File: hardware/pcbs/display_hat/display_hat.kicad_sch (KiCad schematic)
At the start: 6 parts, among them J1 Conn_02x20_Odd_Even

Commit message: hat_pcbs are almost done
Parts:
- removed J1: Conn_02x20_Odd_Even, Connector_PinHeader_2.54mm:PinHeader_2x20_P2.54mm_Vertical, symbol Connector_Generic:Conn_02x20_Odd_Even
- removed J?: I/O, Library:mta100_01x6_P2.54_647050-6, symbol Connector_Generic:Conn_01x06
- added C1: 1μF, Capacitor_SMD:C_0805_2012Metric, symbol Device:C
- added J1: WAVESHARE_HAT_HEADER, Connector_PinHeader_2.54mm:PinHeader_2x20_P2.54mm_Vertical, symbol conn:waveshare_hat_header
- added J2, J3: Header_01x08, Connector_MTA-100:mta100_01x8_P2.54_640455-8, symbol conn:Conn_01x08
- added J4: MTA100_02, Connector_MTA-100:mta100_01x2_P2.54_640455-2, symbol conn:Screw_Terminal_01x02
- added JP1: PWR FROM SIDE, Connector_PinHeader_2.54mm:PinHeader_1x02_P2.54mm_Vertical, symbol Jumper:Jumper_2_Open
- added JP2: PWR FROM MAIN, Connector_PinHeader_2.54mm:PinHeader_1x02_P2.54mm_Vertical, symbol Jumper:Jumper_2_Open
- added R1: 10kΩ, Resistor_SMD:R_0805_2012Metric, symbol Device:R
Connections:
- net +5V: now also J1.2 (+5V), J1.4 (+5V)
- net GND: now also C1.2, J1.14 (GND), J1.20 (GND), J1.25 (GND), J1.30 (GND), J1.34 (GND), J1.39 (GND), J1.6 (GND), J1.9 (GND), J2.1 (Pin_1), J3.8 (Pin_8), J4.1 (Pin_1)
- new net: J2.8 (Pin_8), JP1.1 (A)
- new net: J3.7 (Pin_7), JP2.1 (A)
- new net +3.3V: C1.1, J1.1 (+3.3V), J1.17 (+3.3V), J4.2 (Pin_2), JP1.2 (B), JP2.2 (B), R1.2
- new net BL: J1.32 (D2_BL), J1.33 (D1_BL), J1.35 (D0_BL), J3.2 (Pin_2), R1.1
- new net MAIN_CLK: J1.40 (D0_CLK), J3.4 (Pin_4)
- new net MAIN_CS: J1.12 (D0_CS), J3.6 (Pin_6)
- new net MAIN_DAT: J1.38 (D0_DAT), J3.3 (Pin_3)
- new net MAIN_DC: J1.15 (D0_DC), J3.5 (Pin_5)
- new net MAIN_RST: J1.13 (D0_RST), J3.1 (Pin_1)
- new net SIDE_CLK: J1.23 (D12_CLK), J2.6 (Pin_6)
- new net SIDE_CS_L: J1.24 (D1_CS), J2.4 (Pin_4)
- new net SIDE_CS_R: J1.26 (D2_CS), J2.5 (Pin_5)
- new net SIDE_DAT: J1.19 (D12_DAT), J2.7 (Pin_7)
- new net SIDE_DC: J1.29 (D2_DC), J1.7 (D1_DC), J2.3 (Pin_3)
- new net SIDE_RST: J1.16 (D2_RST), J1.18 (D1_RST), J2.2 (Pin_2)
- no-connect marks 0 -> 12
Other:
- moved on the sheet: H1, H2, H3, H4

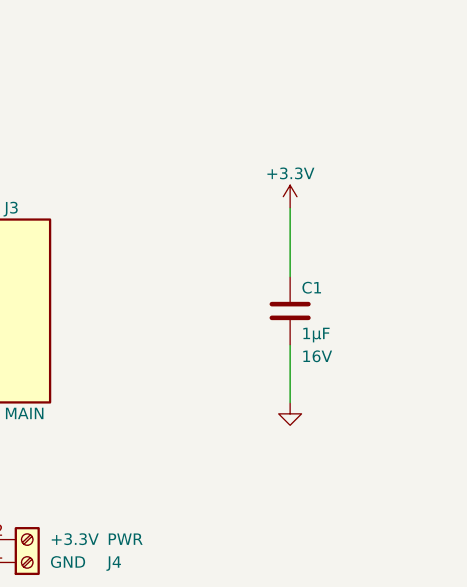
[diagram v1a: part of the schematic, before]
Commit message: hat_pcbs: add some resistors
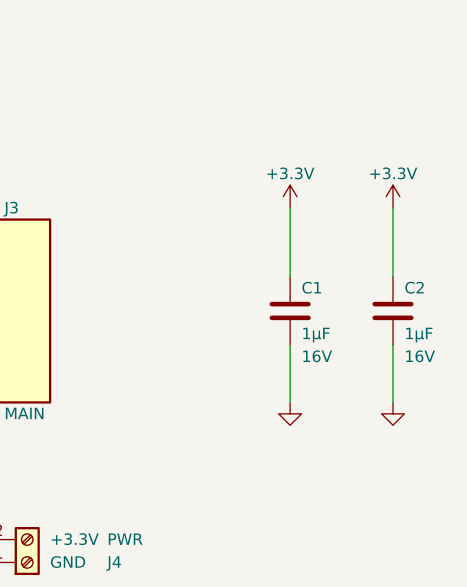
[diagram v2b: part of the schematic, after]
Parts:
- added C2: 1μF, Capacitor_SMD:C_0805_2012Metric, symbol Device:C
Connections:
- net +3.3V: now also C2.1
- net GND: now also C2.2

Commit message: pcbs: update purchase info
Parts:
- J1: Part (none) -> Header_2x20
- J2, J3: value Header_01x08 -> MTA100_08; Part (none) -> 640456-8; Shop (none) -> https://eu.mouser.com/ProductDetail/TE-Connectivity-AMP/640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
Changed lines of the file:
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@@
 		)
 		(instances
-			(project ""
+			(project "display_hat"
 				(path "/052b9242-0509-4017-8d2f-5b1a55978321"
 					(reference "#FLG01")
@@
 			)
 		)
+		(property "Part" "Header_2x20"
+			(at 63.5 71.12 0)
+			(effects
+				(font
+					(size 1.27 1.27)
+				)
+				(hide yes)
+			)
+		)
 		(pin "33"
 		)
@@
 		)
 		(instances
-			(project ""
+			(project "display_hat"
 				(path "/052b9242-0509-4017-8d2f-5b1a55978321"
 					(reference "J1")
@@
 			)
 		)
-		(property "Value" "Header_01x08"
+		(property "Value" "MTA100_08"
 			(at 161.036 109.22 0)
 			(effects
@@
 			)
 		)
+		(property "Part" "640456-8"
+			(at 156.21 127 0)
+			(effects
+				(font
+					(size 1.27 1.27)
+				)
+				(hide yes)
+			)
+		)
+		(property "Shop" "https://eu.mouser.com/ProductDetail/TE-Connectivity-AMP/640456-8?qs=%2F35zJ5USjomho1287DA4QA%3D%3D"
+			(at 156.21 127 0)
+			(effects
+				(font
+					(size 1.27 1.27)
+				)
+				(hide yes)
+			)
+		)
 		(pin "2"
 		)
@@
 			)
 		)
-		(property "Value" "Header_01x08"
+		(property "Value" "MTA100_08"
 			(at 161.036 55.88 0)
 			(effects
@@
 			)
 		)
+		(property "Part" "640456-8"
+			(at 156.21 73.66 0)
+			(effects
+				(font
+					(size 1.27 1.27)
+				)
+				(hide yes)
+			)
+		)
+		(property "Shop" "https://eu.mouser.com/ProductDetail/TE-Connectivity-AMP/640456-8?qs=%2F35zJ5USjomho1287DA4QA%3D%3D"
+			(at 156.21 73.66 0)
+			(effects
+				(font
+					(size 1.27 1.27)
+				)
+				(hide yes)
+			)
+		)
 		(pin "6"
 		)
@@
 		)
 		(instances
-			(project ""
+			(project "display_hat"
 				(path "/052b9242-0509-4017-8d2f-5b1a55978321"
 					(reference "J2")

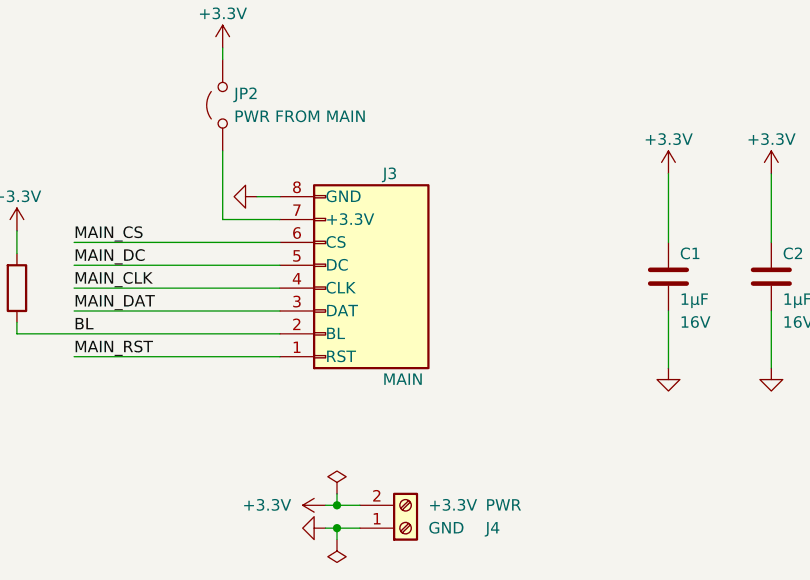
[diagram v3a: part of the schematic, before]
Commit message: boards: fix many silly bugs discovered during testing
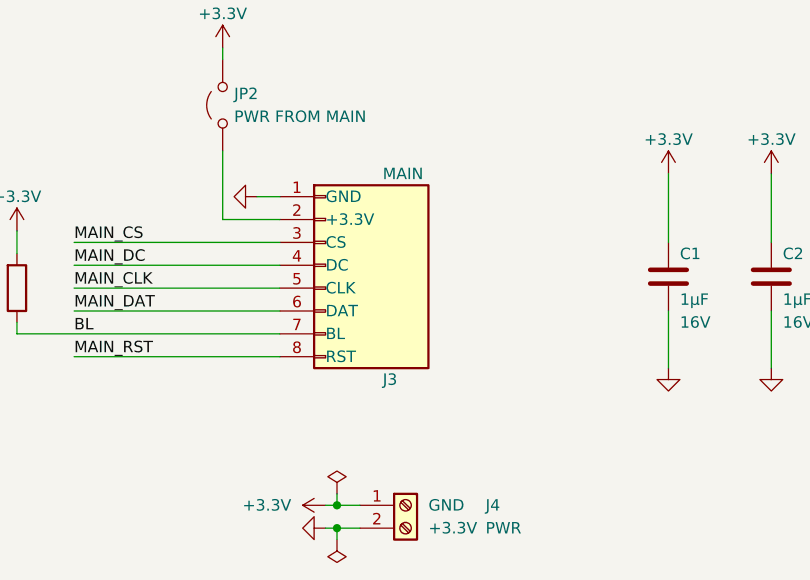
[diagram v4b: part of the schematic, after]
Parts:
- J3: Purpose Pin1 RST -> GND; Purpose Pin2 BL -> +3.3V; Purpose Pin3 DAT -> CS; Purpose Pin4 CLK -> DC; Purpose Pin5 DC -> CLK; Purpose Pin6 CS -> DAT; Purpose Pin7 +3.3V -> BL; Purpose Pin8 GND -> RST
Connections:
- net +3.3V: now also J4.1 (Pin_1); no longer J4.2 (Pin_2)
- net BL: now also J3.7 (Pin_7); no longer J3.2 (Pin_2)
- net GND: now also J3.1 (Pin_1), J4.2 (Pin_2); no longer J3.8 (Pin_8), J4.1 (Pin_1)
- net MAIN_CLK: now also J3.5 (Pin_5); no longer J3.4 (Pin_4)
- net MAIN_CS: now also J3.3 (Pin_3); no longer J3.6 (Pin_6)
- net MAIN_DAT: now also J3.6 (Pin_6); no longer J3.3 (Pin_3)
- net MAIN_DC: now also J3.4 (Pin_4); no longer J3.5 (Pin_5)
- net MAIN_RST: now also J3.8 (Pin_8); no longer J3.1 (Pin_1)
- net at JP2.1 (A): now also J3.2 (Pin_2); no longer J3.7 (Pin_7)
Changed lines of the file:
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@@
 	(symbol
 		(lib_id "conn:Screw_Terminal_01x02")
-		(at 165.1 148.59 0)
-		(mirror x)
+		(at 165.1 146.05 0)
 		(unit 1)
 		(exclude_from_sim no)
@@
 		(dnp no)
 		(property "Reference" "J4"
+			(at 173.99 146.05 0)
+			(effects
+				(font
+					(size 1.27 1.27)
+				)
+				(justify left)
+			)
+		)
+		(property "Value" "MTA100_02"
+			(at 165.1 151.13 0)
+			(effects
+				(font
+					(size 1.27 1.27)
+				)
+				(hide yes)
+			)
+		)
+		(property "Footprint" "Connector_MTA-100:mta100_01x2_P2.54_640455-2"
+			(at 165.1 146.05 0)
+			(effects
+				(font
+					(size 1.27 1.27)
+				)
+				(hide yes)
+			)
+		)
+		(property "Datasheet" "~"
+			(at 165.1 146.05 0)
+			(effects
+				(font
+					(size 1.27 1.27)
+				)
+				(hide yes)
+			)
+		)
+		(property "Description" ""
+			(at 165.1 146.05 0)
+			(effects
+				(font
+					(size 1.27 1.27)
+				)
+				(hide yes)
+			)
+		)
+		(property "Purpose" "PWR"
 			(at 173.99 148.59 0)
 			(effects
@@
 			)
 		)
-		(property "Value" "MTA100_02"
-			(at 165.1 143.51 0)
-			(effects
-				(font
-					(size 1.27 1.27)
-				)
-				(hide yes)
-			)
-		)
-		(property "Footprint" "Connector_MTA-100:mta100_01x2_P2.54_640455-2"
-			(at 165.1 148.59 0)
-			(effects
-				(font
-					(size 1.27 1.27)
-				)
-				(hide yes)
-			)
-		)
-		(property "Datasheet" "~"
-			(at 165.1 148.59 0)
-			(effects
-				(font
-					(size 1.27 1.27)
-				)
-				(hide yes)
-			)
-		)
-		(property "Description" ""
-			(at 165.1 148.59 0)
-			(effects
-				(font
-					(size 1.27 1.27)
-				)
-				(hide yes)
-			)
-		)
-		(property "Purpose" "PWR"
-			(at 173.99 146.05 0)
-			(effects
-				(font
-					(size 1.27 1.27)
-				)
-				(justify left)
-			)
-		)
 		(property "Purpose Pin1" "GND"
+			(at 167.64 146.05 0)
+			(effects
+				(font
+					(size 1.27 1.27)
+				)
+				(justify left)
+			)
+		)
+		(property "Purpose Pin2" "+3.3V"
 			(at 167.64 148.59 0)
 			(effects
@@
 			)
 		)
-		(property "Purpose Pin2" "+3.3V"
-			(at 167.64 146.05 0)
-			(effects
-				(font
-					(size 1.27 1.27)
-				)
-				(justify left)
-			)
-		)
 		(property "Shop" "https://eu.mouser.com/ProductDetail/TE-Connectivity-AMP/640456-2?qs=%2F35zJ5USjomRu3EJQJgZCQ%3D%3D"
-			(at 165.1 148.59 0)
+			(at 165.1 146.05 0)
 			(effects
 				(font
@@
 		)
 		(property "Part" "640456-2"
-			(at 165.1 148.59 0)
+			(at 165.1 146.05 0)
 			(effects
 				(font
@@
 	(symbol
 		(lib_id "conn:Conn_01x08")
-		(at 156.21 127 0)
-		(mirror x)
+		(at 156.21 114.3 0)
 		(unit 1)
 		(exclude_from_sim no)
@@
 		(dnp no)
 		(property "Reference" "J3"
+			(at 162.56 132.08 0)
+			(effects
+				(font
+					(size 1.27 1.27)
+				)
+				(justify left)
+			)
+		)
+		(property "Value" "MTA100_08"
+			(at 161.036 132.08 0)
+			(effects
+				(font
+					(size 1.27 1.27)
+				)
+				(hide yes)
+			)
+		)
+		(property "Footprint" "Connector_MTA-100:mta100_01x8_P2.54_640455-8"
+			(at 156.21 109.982 0)
+			(effects
+				(font
+					(size 1.27 1.27)
+				)
+				(hide yes)
+			)
+		)
+		(property "Datasheet" "~"
+			(at 156.21 114.3 0)
+			(effects
+				(font
+					(size 1.27 1.27)
+				)
+				(hide yes)
+			)
+		)
+		(property "Description" "Generic connector, single row, 01x06, script generated (kicad-library-utils/schlib/autogen/connector/)"
+			(at 156.464 109.982 0)
+			(effects
+				(font
+					(size 1.27 1.27)
+				)
+				(hide yes)
+			)
+		)
+		(property "Purpose Pin1" "GND"
+			(at 156.21 111.76 0)
+			(do_not_autoplace yes)
+			(effects
+				(font
+					(size 1.27 1.27)
+				)
+				(justify left)
+			)
+		)
+		(property "Purpose Pin2" "+3.3V"
+			(at 156.21 114.3 0)
+			(do_not_autoplace yes)
+			(effects
+				(font
+					(size 1.27 1.27)
+				)
+				(justify left)
+			)
+		)
+		(property "Purpose Pin3" "CS"
+			(at 156.21 116.84 0)
+			(do_not_autoplace yes)
+			(effects
+				(font
+					(size 1.27 1.27)
+				)
+				(justify left)
+			)
+		)
+		(property "Purpose Pin4" "DC"
+			(at 156.21 119.38 0)
+			(do_not_autoplace yes)
+			(effects
+				(font
+					(size 1.27 1.27)
+				)
+				(justify left)
+			)
+		)
+		(property "Purpose Pin5" "CLK"
+			(at 156.21 121.92 0)
+			(do_not_autoplace yes)
+			(effects
+				(font
+					(size 1.27 1.27)
+				)
+				(justify left)
+			)
+		)
+		(property "Purpose Pin6" "DAT"
+			(at 156.21 124.46 0)
+			(do_not_autoplace yes)
+			(effects
+				(font
+					(size 1.27 1.27)
+				)
+				(justify left)
+			)
+		)
+		(property "Purpose Pin7" "BL"
+			(at 156.21 127 0)
+			(do_not_autoplace yes)
+			(effects
+				(font
+					(size 1.27 1.27)
+				)
+				(justify left)
+			)
+		)
+		(property "Purpose Pin8" "RST"
+			(at 156.21 129.54 0)
+			(do_not_autoplace yes)
+			(effects
+				(font
+					(size 1.27 1.27)
+				)
+				(justify left)
+			)
+		)
+		(property "Purpose" "MAIN"
 			(at 162.56 109.22 0)
 			(effects
@@
 			)
 		)
-		(property "Value" "MTA100_08"
-			(at 161.036 109.22 0)
-			(effects
-				(font
-					(size 1.27 1.27)
-				)
-				(hide yes)
-			)
-		)
-		(property "Footprint" "Connector_MTA-100:mta100_01x8_P2.54_640455-8"
-			(at 156.21 131.318 0)
-			(effects
-				(font
-					(size 1.27 1.27)
-				)
-				(hide yes)
-			)
-		)
-		(property "Datasheet" "~"
-			(at 156.21 127 0)
-			(effects
-				(font
-					(size 1.27 1.27)
-				)
-				(hide yes)
-			)
-		)
-		(property "Description" "Generic connector, single row, 01x06, script generated (kicad-library-utils/schlib/autogen/connector/)"
-			(at 156.464 131.318 0)
-			(effects
-				(font
-					(size 1.27 1.27)
-				)
-				(hide yes)
-			)
-		)
-		(property "Purpose Pin1" "RST"
-			(at 156.21 129.54 0)
-			(do_not_autoplace yes)
-			(effects
-				(font
-					(size 1.27 1.27)
-				)
-				(justify left)
-			)
-		)
-		(property "Purpose Pin2" "BL"
-			(at 156.21 127 0)
-			(do_not_autoplace yes)
-			(effects
-				(font
-					(size 1.27 1.27)
-				)
-				(justify left)
-			)
-		)
-		(property "Purpose Pin3" "DAT"
-			(at 156.21 124.46 0)
-			(do_not_autoplace yes)
-			(effects
-				(font
-					(size 1.27 1.27)
-				)
-				(justify left)
-			)
-		)
-		(property "Purpose Pin4" "CLK"
-			(at 156.21 121.92 0)
-			(do_not_autoplace yes)
-			(effects
-				(font
-					(size 1.27 1.27)
-				)
-				(justify left)
-			)
-		)
-		(property "Purpose Pin5" "DC"
-			(at 156.21 119.38 0)
-			(do_not_autoplace yes)
-			(effects
-				(font
-					(size 1.27 1.27)
-				)
-				(justify left)
-			)
-		)
-		(property "Purpose Pin6" "CS"
-			(at 156.21 116.84 0)
-			(do_not_autoplace yes)
-			(effects
-				(font
-					(size 1.27 1.27)
-				)
-				(justify left)
-			)
-		)
-		(property "Purpose Pin7" "+3.3V"
+		(property "Part" "640456-8"
 			(at 156.21 114.3 0)
-			(do_not_autoplace yes)
-			(effects
-				(font
-					(size 1.27 1.27)
-				)
-				(justify left)
-			)
-		)
-		(property "Purpose Pin8" "GND"
-			(at 156.21 111.76 0)
-			(do_not_autoplace yes)
-			(effects
-				(font
-					(size 1.27 1.27)
-				)
-				(justify left)
-			)
-		)
-		(property "Purpose" "MAIN"
-			(at 162.56 132.08 0)
-			(effects
-				(font
-					(size 1.27 1.27)
-				)
-				(justify left)
-			)
-		)
-		(property "Part" "640456-8"
-			(at 156.21 127 0)
 			(effects
 				(font
@@
 		)
 		(property "Shop" "https://eu.mouser.com/ProductDetail/TE-Connectivity-AMP/640456-8?qs=%2F35zJ5USjomho1287DA4QA%3D%3D"
-			(at 156.21 127 0)
-			(effects
-				(font
+			(at 156.21 114.3 0)
+			(effects
+				(font
